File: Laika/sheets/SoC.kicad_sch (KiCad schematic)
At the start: 1 part, among them U1 Milk-V Duo Module

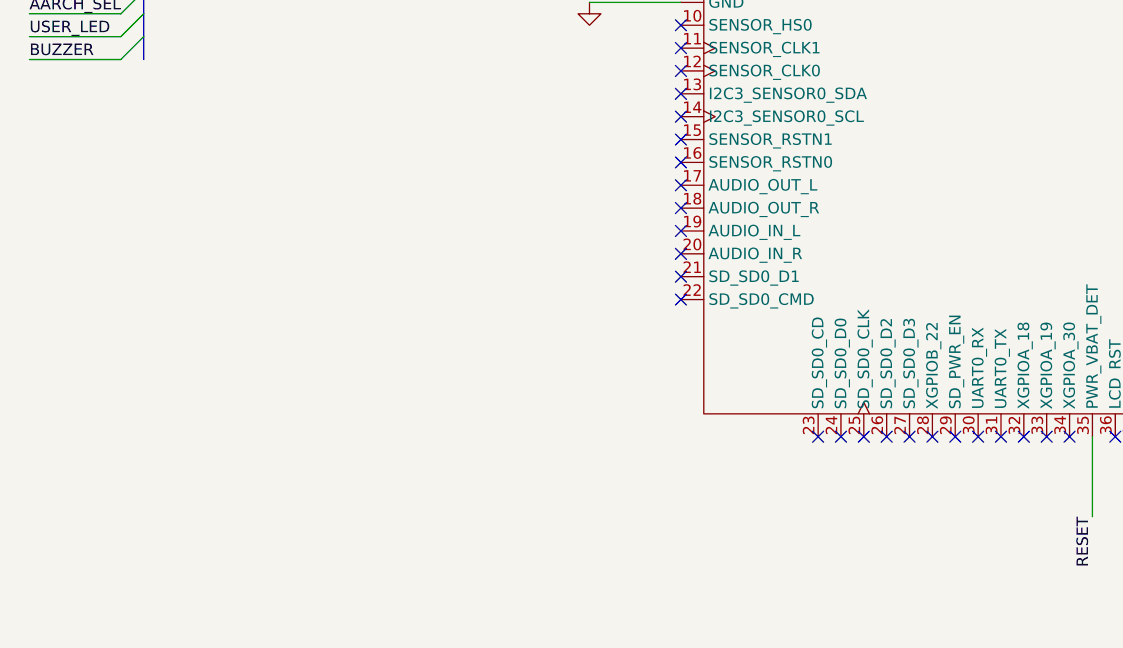
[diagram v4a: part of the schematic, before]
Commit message: Added SD card power source selector and boot medium selector.
The SD card power source (VDD_SD) can be selected between a software
managed 3.3V power supply (PWR_SD_SW); or through the 3.3V power rail
(+3V3). Doubles as selector whether to boot from SD card or eMMC.
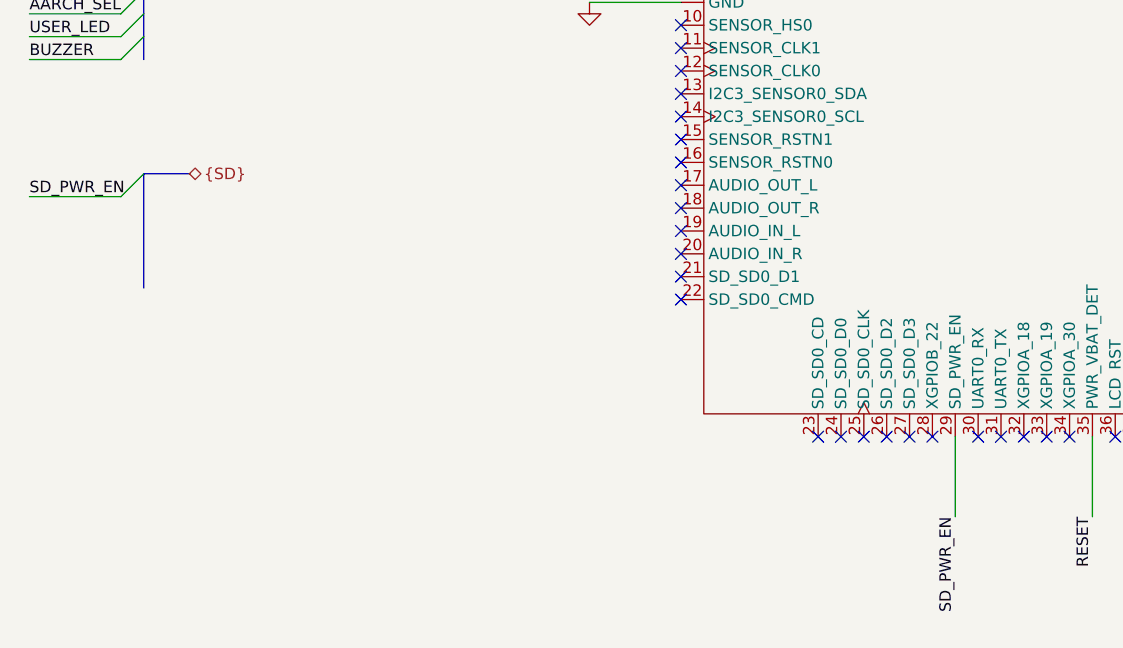
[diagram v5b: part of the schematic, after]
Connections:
- net SD_PWR_EN: now reaches U1.29 (SD_PWR_EN)
- no-connect marks 76 -> 75
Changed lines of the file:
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@@
-	)
-	(no_connect
-		(at 128.27 143.51)
 	)
 	(no_connect
@@
 	)
 	(bus_entry
+		(at 38.1 114.3)
+		(size -2.54 2.54)
+		(stroke
+			(width 0)
+			(type default)
+		)
+	)
+	(bus_entry
 		(at 38.1 93.98)
 		(size -2.54 2.54)
@@
 	(wire
 		(pts
+			(xy 128.27 152.4) (xy 128.27 143.51)
+		)
+		(stroke
+			(width 0)
+			(type default)
+		)
+	)
+	(wire
+		(pts
 			(xy 143.51 152.4) (xy 143.51 143.51)
 		)
@@
 	(wire
 		(pts
+			(xy 25.4 116.84) (xy 35.56 116.84)
+		)
+		(stroke
+			(width 0)
+			(type default)
+		)
+	)
+	(wire
+		(pts
 			(xy 25.4 99.06) (xy 35.56 99.06)
 		)
@@
 		)
 	)
+	(bus
+		(pts
+			(xy 43.18 114.3) (xy 38.1 114.3)
+		)
+		(stroke
+			(width 0)
+			(type default)
+		)
+	)
 	(wire
 		(pts
@@
 		(pts
 			(xy 38.1 73.66) (xy 38.1 76.2)
+		)
+		(stroke
+			(width 0)
+			(type default)
+		)
+	)
+	(bus
+		(pts
+			(xy 38.1 114.3) (xy 38.1 127)
 		)
 		(stroke
@@
 		)
 	)
+	(label "SD_PWR_EN"
+		(at 128.27 152.4 270)
+		(effects
+			(font
+				(size 1.27 1.27)
+			)
+			(justify right bottom)
+		)
+	)
 	(label "USB_DM"
 		(at 190.5 77.47 0)
@@
 	(label "BUZZER"
 		(at 25.4 101.6 0)
+		(effects
+			(font
+				(size 1.27 1.27)
+			)
+			(justify left bottom)
+		)
+	)
+	(label "SD_PWR_EN"
+		(at 25.4 116.84 0)
 		(effects
 			(font
@@
 		(effects
 			(font
+				(size 1.27 1.27)
+			)
+			(justify left)
+		)
+	)
+	(hierarchical_label "{SD}"
+		(shape bidirectional)
+		(at 43.18 114.3 0)
+		(effects
+			(font

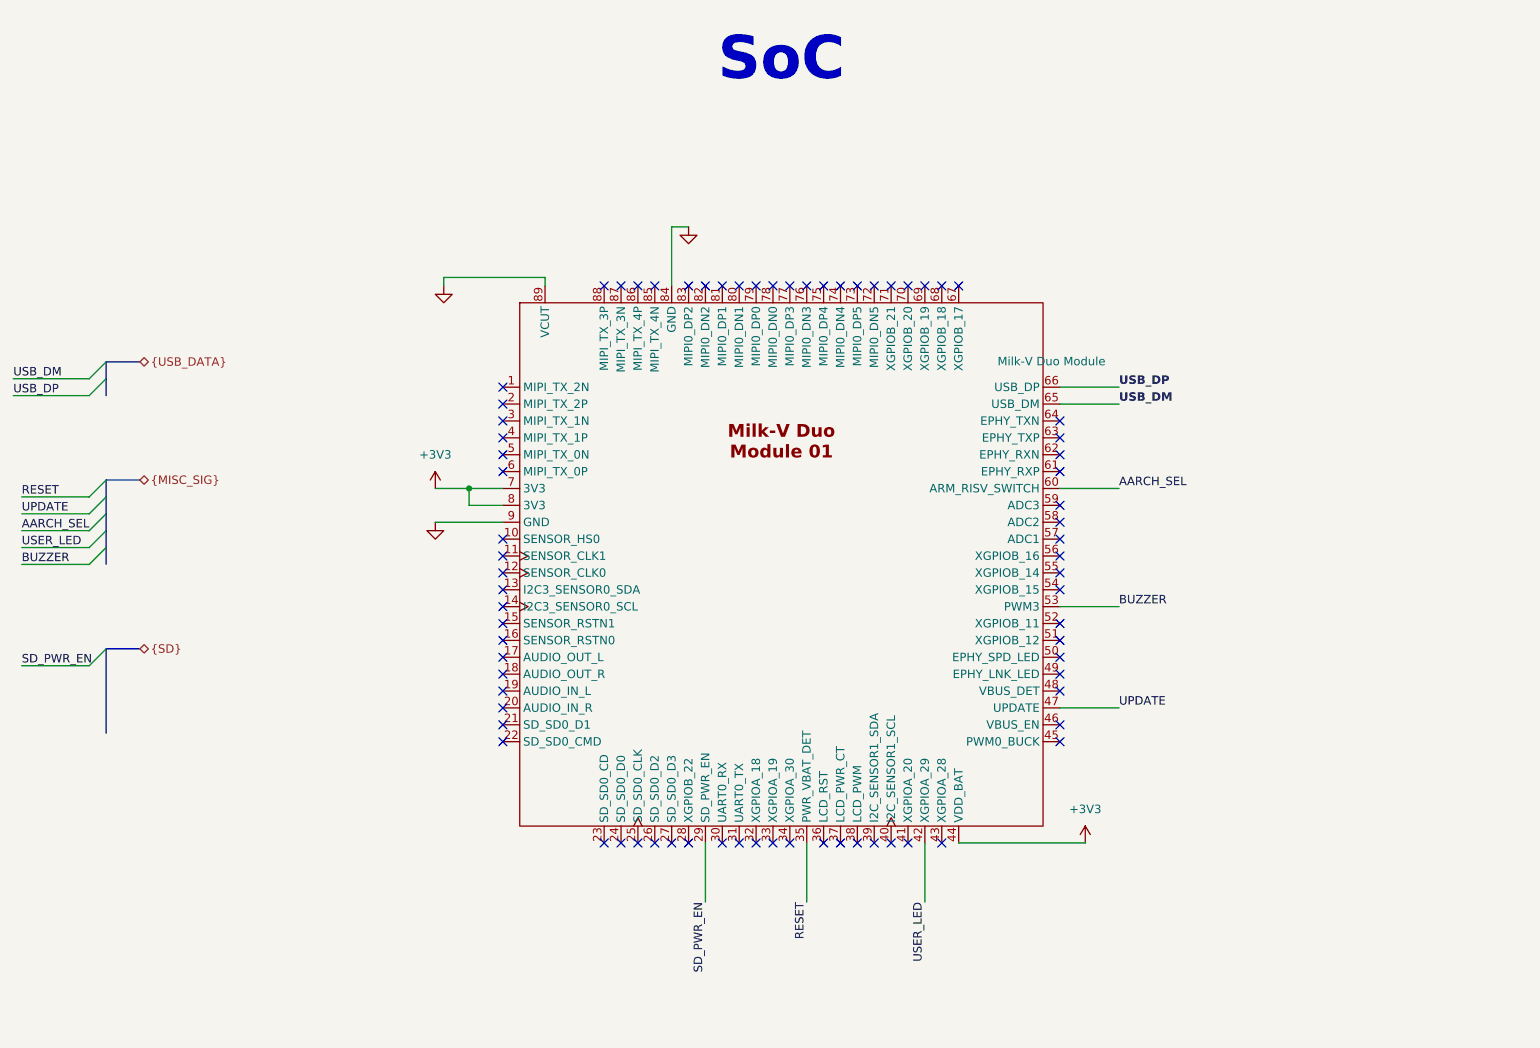
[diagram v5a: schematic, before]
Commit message: Completed microSD card receptacle block
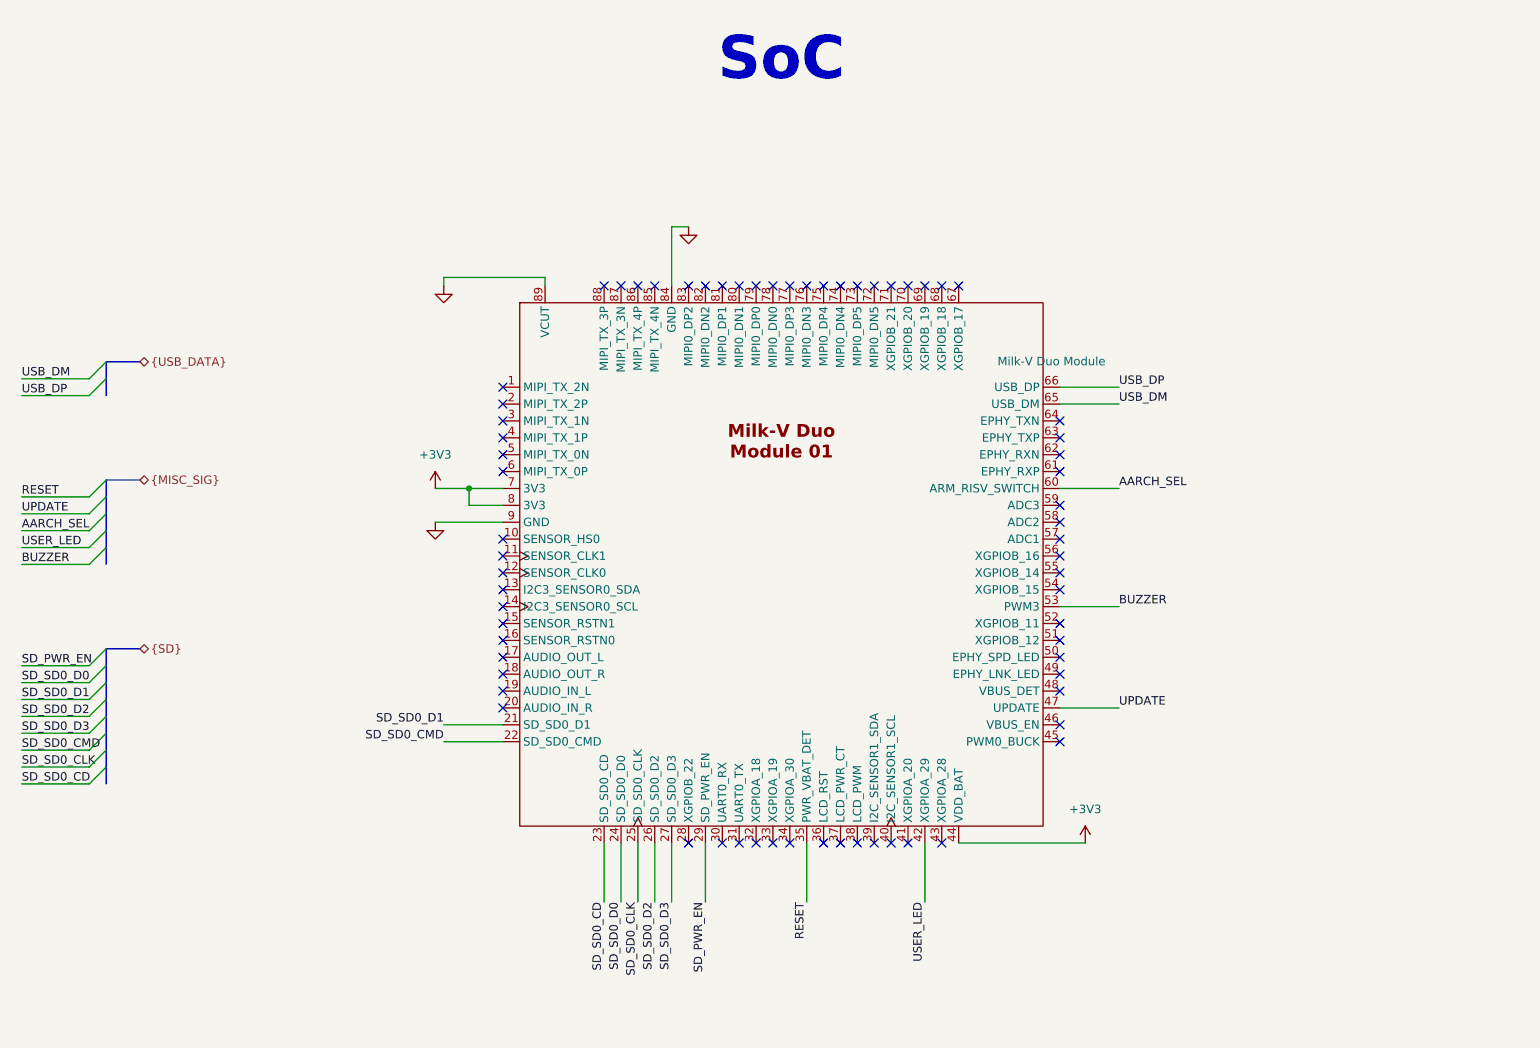
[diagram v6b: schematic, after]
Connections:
- net SD_SD0_D1: now reaches U1.21 (SD_SD0_D1)
- net SD_SD0_CMD: now reaches U1.22 (SD_SD0_CMD)
- net SD_SD0_CD: now reaches U1.23 (SD_SD0_CD)
- net SD_SD0_D0: now reaches U1.24 (SD_SD0_D0)
- net SD_SD0_CLK: now reaches U1.25 (SD_SD0_CLK)
- net SD_SD0_D2: now reaches U1.26 (SD_SD0_D2)
- net SD_SD0_D3: now reaches U1.27 (SD_SD0_D3)
- no-connect marks 75 -> 68

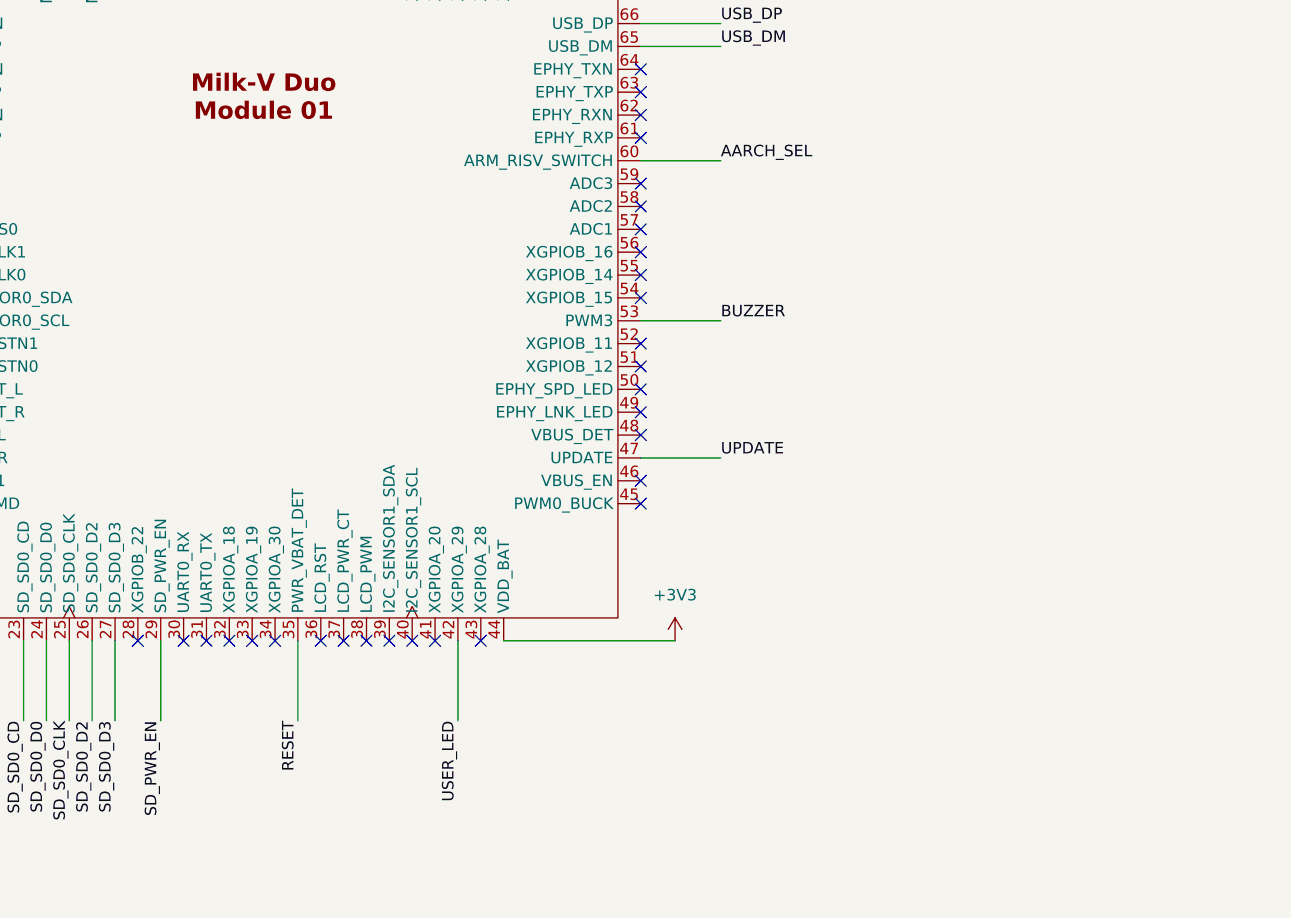
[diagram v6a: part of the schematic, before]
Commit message: Added headers for system uart console. DNP for SD CLK.
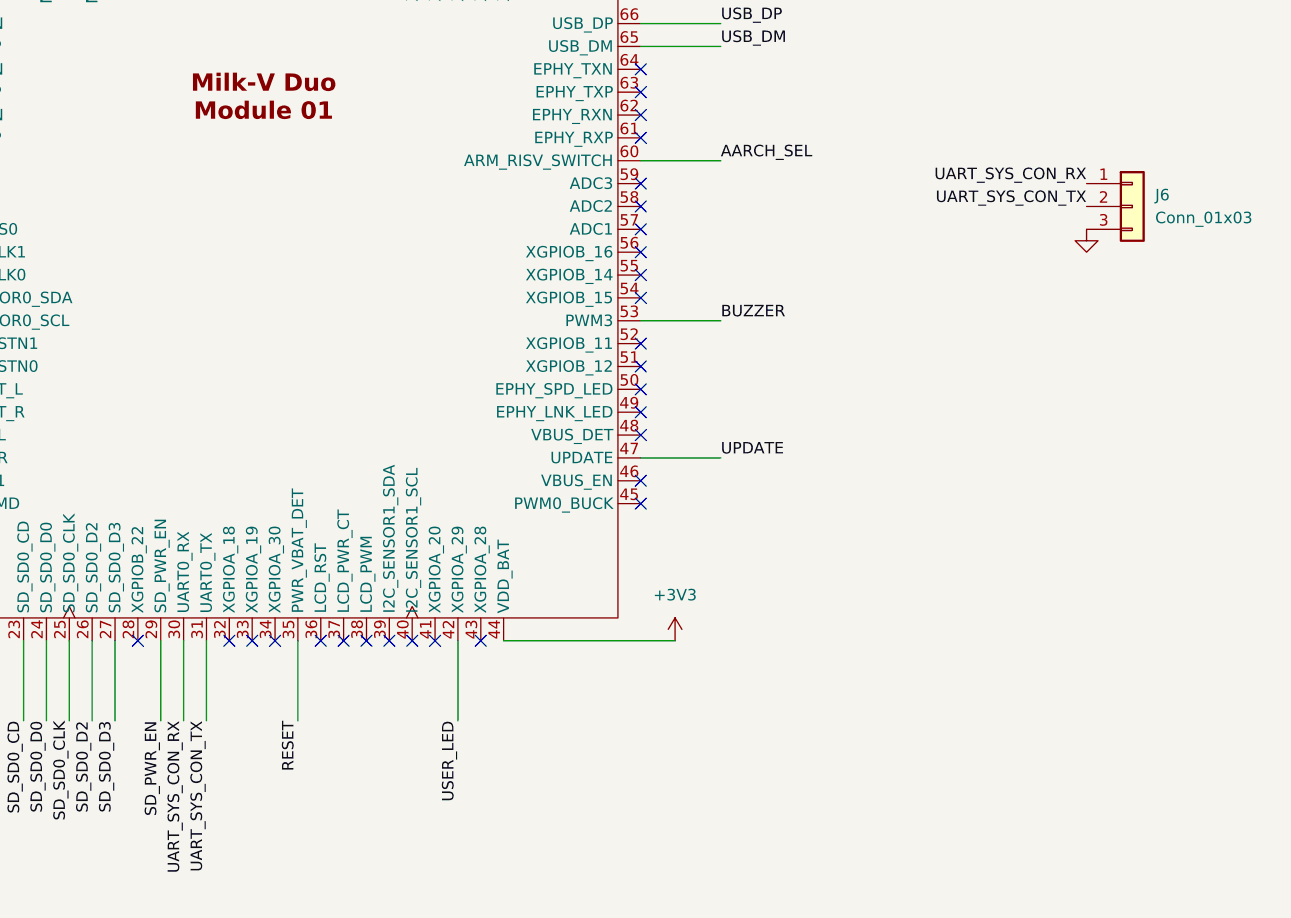
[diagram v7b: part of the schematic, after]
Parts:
- added J6: Conn_01x03, symbol Connector_Generic:Conn_01x03
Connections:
- net GND: now also J6.3 (Pin_3)
- net UART_SYS_CON_RX: now reaches U1.30 (UART0_RX)
- net UART_SYS_CON_RX: now also J6.1 (Pin_1)
- net UART_SYS_CON_TX: now reaches U1.31 (UART0_TX)
- net UART_SYS_CON_TX: now also J6.2 (Pin_2)
- no-connect marks 68 -> 66
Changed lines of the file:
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@@
-	)
-	(no_connect
-		(at 130.81 143.51)
 	)
 	(no_connect
@@
 	(no_connect
 		(at 148.59 59.69)
-	)
-	(no_connect
-		(at 133.35 143.51)
 	)
 	(no_connect
@@
 	(wire
 		(pts
+			(xy 133.35 143.51) (xy 133.35 152.4)
+		)
+		(stroke
+			(width 0)
+			(type default)
+		)
+	)
+	(wire
+		(pts
 			(xy 25.4 119.38) (xy 35.56 119.38)
 		)
@@
 		(pts
 			(xy 120.65 143.51) (xy 120.65 152.4)
+		)
+		(stroke
+			(width 0)
+			(type default)
+		)
+	)
+	(wire
+		(pts
+			(xy 130.81 152.4) (xy 130.81 143.51)
 		)
 		(stroke
@@
 		)
 	)
+	(label "UART_SYS_CON_TX"
+		(at 231.14 95.25 180)
+		(effects
+			(font
+				(size 1.27 1.27)
+			)
+			(justify right bottom)
+		)
+	)
 	(label "SD_SD0_D0"
 		(at 25.4 119.38 0)
@@
 		)
 	)
+	(label "UART_SYS_CON_RX"
+		(at 231.14 92.71 180)
+		(effects
+			(font
+				(size 1.27 1.27)
+			)
+			(justify right bottom)
+		)
+	)
 	(label "USB_DM"
 		(at 190.5 77.47 0)
@@
 		)
 	)
+	(label "UART_SYS_CON_RX"
+		(at 130.81 152.4 270)
+		(effects
+			(font
+				(size 1.27 1.27)
+			)
+			(justify right bottom)
+		)
+	)
 	(label "USB_DP"
 		(at 190.5 74.93 0)
@@
 	(label "USER_LED"
 		(at 161.29 152.4 270)
+		(effects
+			(font
+				(size 1.27 1.27)
+			)
+			(justify right bottom)
+		)
+	)
+	(label "UART_SYS_CON_TX"
+		(at 133.35 152.4 270)
 		(effects
 			(font
@@
 	(symbol
 		(lib_id "power:GND")
+		(at 231.14 97.79 0)
+		(unit 1)
+		(exclude_from_sim no)
+		(in_bom yes)
+		(on_board yes)
+		(dnp no)
+		(fields_autoplaced yes)
+		(property "Reference" "#PWR059"
+			(at 231.14 104.14 0)
+			(effects
+				(font
+					(size 1.27 1.27)
+				)
+				(hide yes)
+			)
+		)
+		(property "Value" "GND"
+			(at 231.14 102.87 0)
+			(effects
+				(font
+					(size 1.27 1.27)
+				)
+				(hide yes)
+			)
+		)
+		(property "Footprint" ""
+			(at 231.14 97.79 0)
+			(effects
+				(font
+					(size 1.27 1.27)
+				)
+				(hide yes)
+			)
+		)
+		(property "Datasheet" ""
+			(at 231.14 97.79 0)
+			(effects
+				(font
+					(size 1.27 1.27)
+				)
+				(hide yes)
+			)
+		)
+		(property "Description" "Power symbol creates a global label with name \"GND\" , ground"
+			(at 231.14 97.79 0)
+			(effects
+				(font
+					(size 1.27 1.27)
+				)
+				(hide yes)
+			)
+		)
+		(pin "1"
+		)
+		(instances
+			(project "Laika"
+				(path "/57baccbf-5d29-4714-8f2e-7e9f593fcdf8/6c078d98-f795-4bff-ba6d-ace5d579e960/afb454cc-1c16-4ce4-9f1e-961c69cee3bb"
+					(reference "#PWR059")
+					(unit 1)
+				)
+			)
+		)
+	)
+	(symbol
+		(lib_id "power:GND")
 		(at 125.73 50.8 0)
 		(unit 1)
@@
 					(unit 1)
 				)
+			)
+		)
+	)
+	(symbol
+		(lib_id "Connector_Generic:Conn_01x03")
+		(at 236.22 95.25 0)
+		(unit 1)
+		(exclude_from_sim no)
+		(in_bom yes)
+		(on_board yes)
+		(dnp no)
+		(fields_autoplaced yes)
+		(property "Reference" "J6"
+			(at 238.76 93.9799 0)
+			(effects
+				(font
+					(size 1.27 1.27)
+				)
+				(justify left)
+			)
+		)
+		(property "Value" "Conn_01x03"
+			(at 238.76 96.5199 0)
+			(effects
+				(font
+					(size 1.27 1.27)
+				)
+				(justify left)
+			)
+		)
+		(property "Footprint" ""
+			(at 236.22 95.25 0)
+			(effects
+				(font
+					(size 1.27 1.27)
+				)
+				(hide yes)
+			)
+		)
+		(property "Datasheet" "~"
+			(at 236.22 95.25 0)
+			(effects
+				(font
+					(size 1.27 1.27)
+				)
+				(hide yes)
+			)
+		)
+		(property "Description" "Generic connector, single row, 01x03, script generated (kicad-library-utils/schlib/autogen/connector/)"
+			(at 236.22 95.25 0)
+			(effects
+				(font
+					(size 1.27 1.27)
+				)
+				(hide yes)
+			)
+		)
+		(pin "1"
+		)
+		(pin "2"
+		)
+		(pin "3"
+		)
+		(instances
+			(project ""
+				(path "/57baccbf-5d29-4714-8f2e-7e9f593fcdf8/6c078d98-f795-4bff-ba6d-ace5d579e960/afb454cc-1c16-4ce4-9f1e-961c69cee3bb"
+					(reference "J6")
+					(unit 1)
+				)
